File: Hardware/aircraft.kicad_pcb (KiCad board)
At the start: 4 copper layers, 131 parts, among them U1 MIC26903YJL-TR, U10 BMP390, U12 STM32F405RGTx, U14 24CW1280T-I/OT, U15 PCA9685PW_118, U16 CH330N, U17 CH330N, U2 LD39200PU33R, U3 INA226, U4 STM32F405RGTx, U5 IST8310, U6 NEO-M8N, U7 BMI088, U8 TMP100, U9 24CW1280T-I/OT

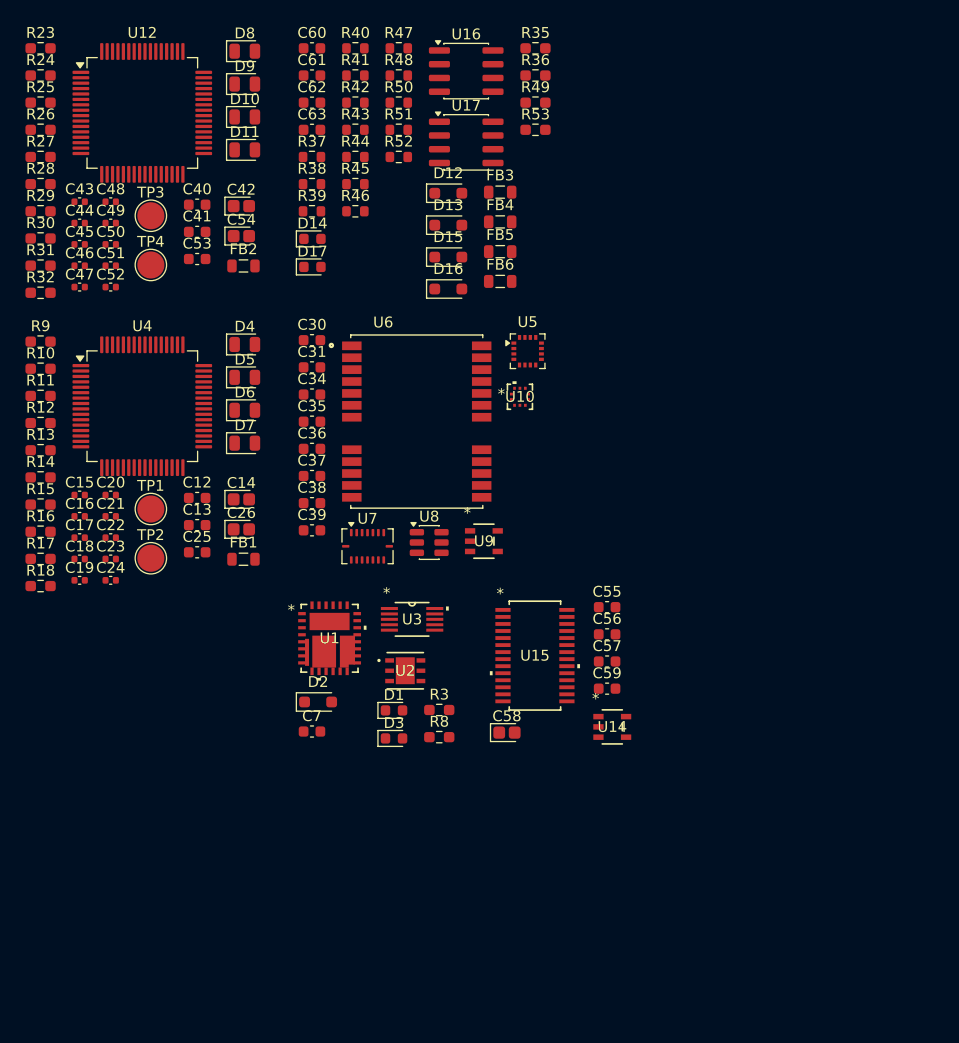
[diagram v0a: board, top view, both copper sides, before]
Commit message: hardware version 0.1.2, minor improvements and footprint selection (missing some gnss and bulk regulator components
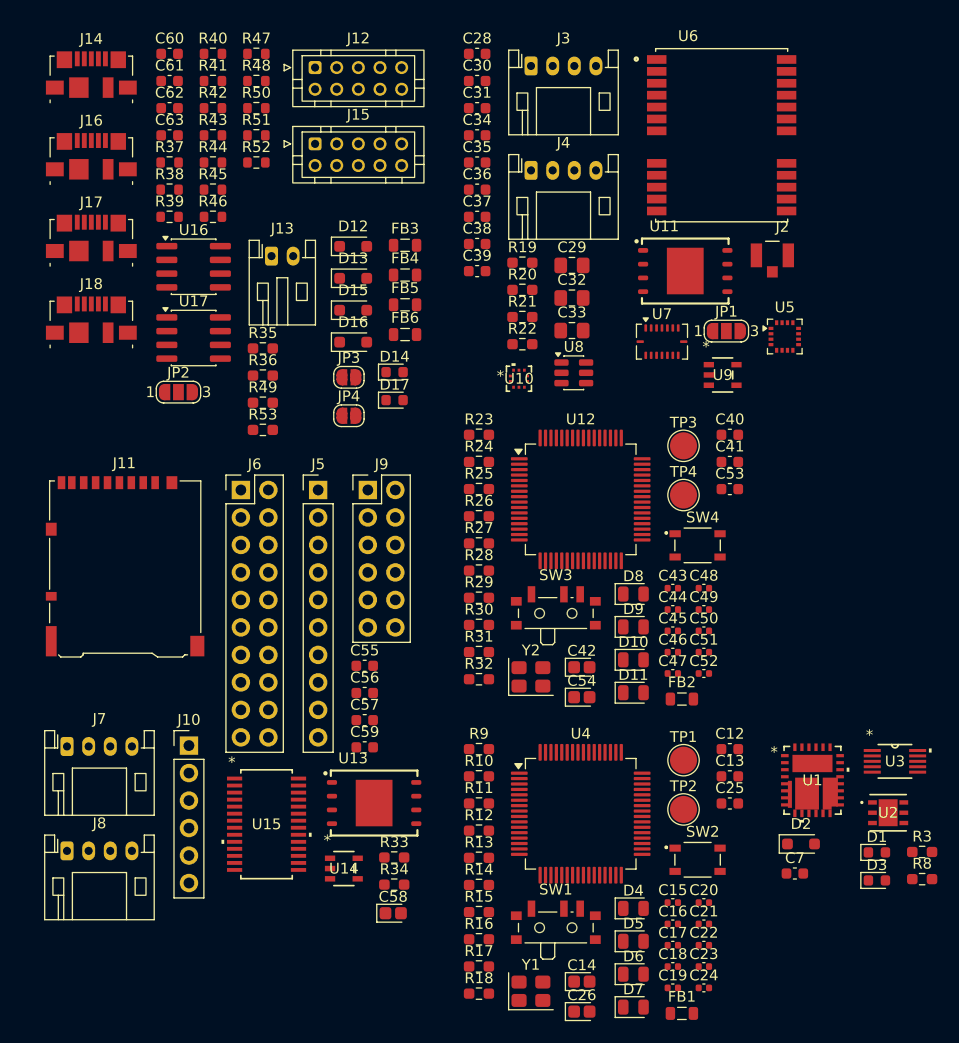
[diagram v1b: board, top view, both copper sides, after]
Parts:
- added C28: 22p, Capacitor_SMD:C_0603_1608Metric, F.Cu at (66.0, 21.7)
- added C29: 4u7, Capacitor_SMD:C_0805_2012Metric_Pad1.18x1.45mm_HandSolder, F.Cu at (74.7, 41.3)
- added C32: 1u, Capacitor_SMD:C_0805_2012Metric_Pad1.18x1.45mm_HandSolder, F.Cu at (74.7, 44.3)
- added C33: 1u, Capacitor_SMD:C_0805_2012Metric_Pad1.18x1.45mm_HandSolder, F.Cu at (74.7, 47.3)
- added J10: Conn_01x06, Connector_PinHeader_2.54mm:PinHeader_1x06_P2.54mm_Vertical, F.Cu at (39.3, 85.7)
- added J11: Micro_SD_Card_Det1, Connector_Card:microSD_HC_Hirose_DM3AT-SF-PEJM5, F.Cu at (33.4, 69.1)
- added J12: Conn_02x05_Odd_Even, Aircraft_Footprints:JST_PHD_B10B-PHDSS_2x05_P2.00mm_Vertical, F.Cu at (51.0, 23.0)
- added J13: Conn_01x02, Connector_JST:JST_PH_S2B-PH-K_1x02_P2.00mm_Horizontal, F.Cu at (47.0, 40.4)
- added J14: USB_B_Micro, Connector_USB:USB_Micro-B_Molex_47346-0001, F.Cu at (30.3, 23.7)
- added J15: Conn_02x05_Odd_Even, Aircraft_Footprints:JST_PHD_B10B-PHDSS_2x05_P2.00mm_Vertical, F.Cu at (51.0, 30.1)
- added J16: USB_B_Micro, Connector_USB:USB_Micro-B_Molex_47346-0001, F.Cu at (30.3, 31.2)
- added J17: USB_B_Micro, Connector_USB:USB_Micro-B_Molex_47346-0001, F.Cu at (30.3, 38.8)
- added J18: USB_B_Micro, Connector_USB:USB_Micro-B_Molex_47346-0001, F.Cu at (30.3, 46.3)
- added J2: 5-1814832-1, Aircraft_Footprints:HIROSE_U.FL-R-SMT-1_80_, F.Cu at (93.2, 40.4)
- added J3: Conn_01x04, Connector_JST:JST_PH_S4B-PH-K_1x04_P2.00mm_Horizontal, F.Cu at (70.9, 22.9)
- added J4: Conn_01x04, Connector_JST:JST_PH_S4B-PH-K_1x04_P2.00mm_Horizontal, F.Cu at (70.9, 32.5)
- added J5: Conn_01x10, Connector_PinHeader_2.54mm:PinHeader_1x10_P2.54mm_Vertical, F.Cu at (51.3, 62.0)
- added J6: Conn_02x10_Odd_Even, Connector_PinHeader_2.54mm:PinHeader_2x10_P2.54mm_Vertical, F.Cu at (44.1, 62.0)
- added J7: Conn_01x04, Connector_JST:JST_PH_S4B-PH-K_1x04_P2.00mm_Horizontal, F.Cu at (28.1, 85.7)
- added J8: Conn_01x04, Connector_JST:JST_PH_S4B-PH-K_1x04_P2.00mm_Horizontal, F.Cu at (28.1, 95.4)
- added J9: Conn_02x06_Odd_Even, Connector_PinHeader_2.54mm:PinHeader_2x06_P2.54mm_Vertical, F.Cu at (55.9, 62.0)
- added JP1: SolderJumper_3_Open, Jumper:SolderJumper-3_P1.3mm_Open_RoundedPad1.0x1.5mm_NumberLabels, F.Cu at (89.0, 47.4)
- added JP2: Jumper_3_Open, Jumper:SolderJumper-3_P1.3mm_Open_RoundedPad1.0x1.5mm_NumberLabels, F.Cu at (38.4, 53.0)
- added JP3: SolderJumper_2_Open, Jumper:SolderJumper-2_P1.3mm_Open_RoundedPad1.0x1.5mm, F.Cu at (54.1, 51.6)
- added JP4: SolderJumper_2_Open, Jumper:SolderJumper-2_P1.3mm_Open_RoundedPad1.0x1.5mm, F.Cu at (54.1, 55.2)
- added R19: 10, Resistor_SMD:R_0603_1608Metric_Pad0.98x0.95mm_HandSolder, F.Cu at (70.1, 41.0)
- added R20: 10k, Resistor_SMD:R_0603_1608Metric_Pad0.98x0.95mm_HandSolder, F.Cu at (70.1, 43.5)
- added R21: 10k, Resistor_SMD:R_0603_1608Metric_Pad0.98x0.95mm_HandSolder, F.Cu at (70.1, 46.1)
- added R22: 10k, Resistor_SMD:R_0603_1608Metric_Pad0.98x0.95mm_HandSolder, F.Cu at (70.1, 48.6)
- added R33: 10k, Resistor_SMD:R_0603_1608Metric_Pad0.98x0.95mm_HandSolder, F.Cu at (58.3, 96.0)
- added R34: 10k, Resistor_SMD:R_0603_1608Metric_Pad0.98x0.95mm_HandSolder, F.Cu at (58.3, 98.5)
- added SW1: SW_SPDT, Button_Switch_SMD:SW_SPDT_PCM12, F.Cu at (73.2, 102.2)
- added SW2: SW_Push_Dual, Aircraft_Footprints:SW_SKRPACE010, F.Cu at (86.3, 96.2)
- added SW3: SW_SPDT, Button_Switch_SMD:SW_SPDT_PCM12, F.Cu at (73.2, 73.1)
- added SW4: SW_Push_Dual, Aircraft_Footprints:SW_SKRPACE010, F.Cu at (86.3, 67.2)
- added U11: W25N01GVZEIG_TR, Aircraft_Footprints:SON127P800X600X80-9N, F.Cu at (85.2, 41.8)
- added U13: W25N01GVZEIG_TR, Aircraft_Footprints:SON127P800X600X80-9N, F.Cu at (56.4, 91.0)
- added Y1: 25MHz, Crystal:Crystal_SMD_Abracon_ABM8G-4Pin_3.2x2.5mm, F.Cu at (70.9, 108.4)
- added Y2: 25MHz, Crystal:Crystal_SMD_Abracon_ABM8G-4Pin_3.2x2.5mm, F.Cu at (70.9, 79.3)
- moved C15 66.5 mm to (84.0, 100.2)
- moved C20 66.5 mm to (86.9, 100.2)
- moved C16 66.5 mm to (84.0, 102.1)
- moved C17 66.5 mm to (84.0, 104.1)
- moved C18 66.5 mm to (84.0, 106.1)
- moved C19 66.5 mm to (84.0, 108.0)
- moved C21 66.5 mm to (86.9, 102.1)
- moved C22 66.5 mm to (86.9, 104.1)
- moved C23 66.5 mm to (86.9, 106.1)
- moved C24 66.5 mm to (86.9, 108.0)
- moved C43 65.4 mm to (84.0, 71.1)
- moved C44 65.4 mm to (84.0, 73.1)
- moved C45 65.4 mm to (84.0, 75.1)
- moved C46 65.4 mm to (84.0, 77.0)
- moved C47 65.4 mm to (84.0, 79.0)
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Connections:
- U6 pad 7: unconnected-(U6-VDD_USB-Pad7) -> PS_PVIN

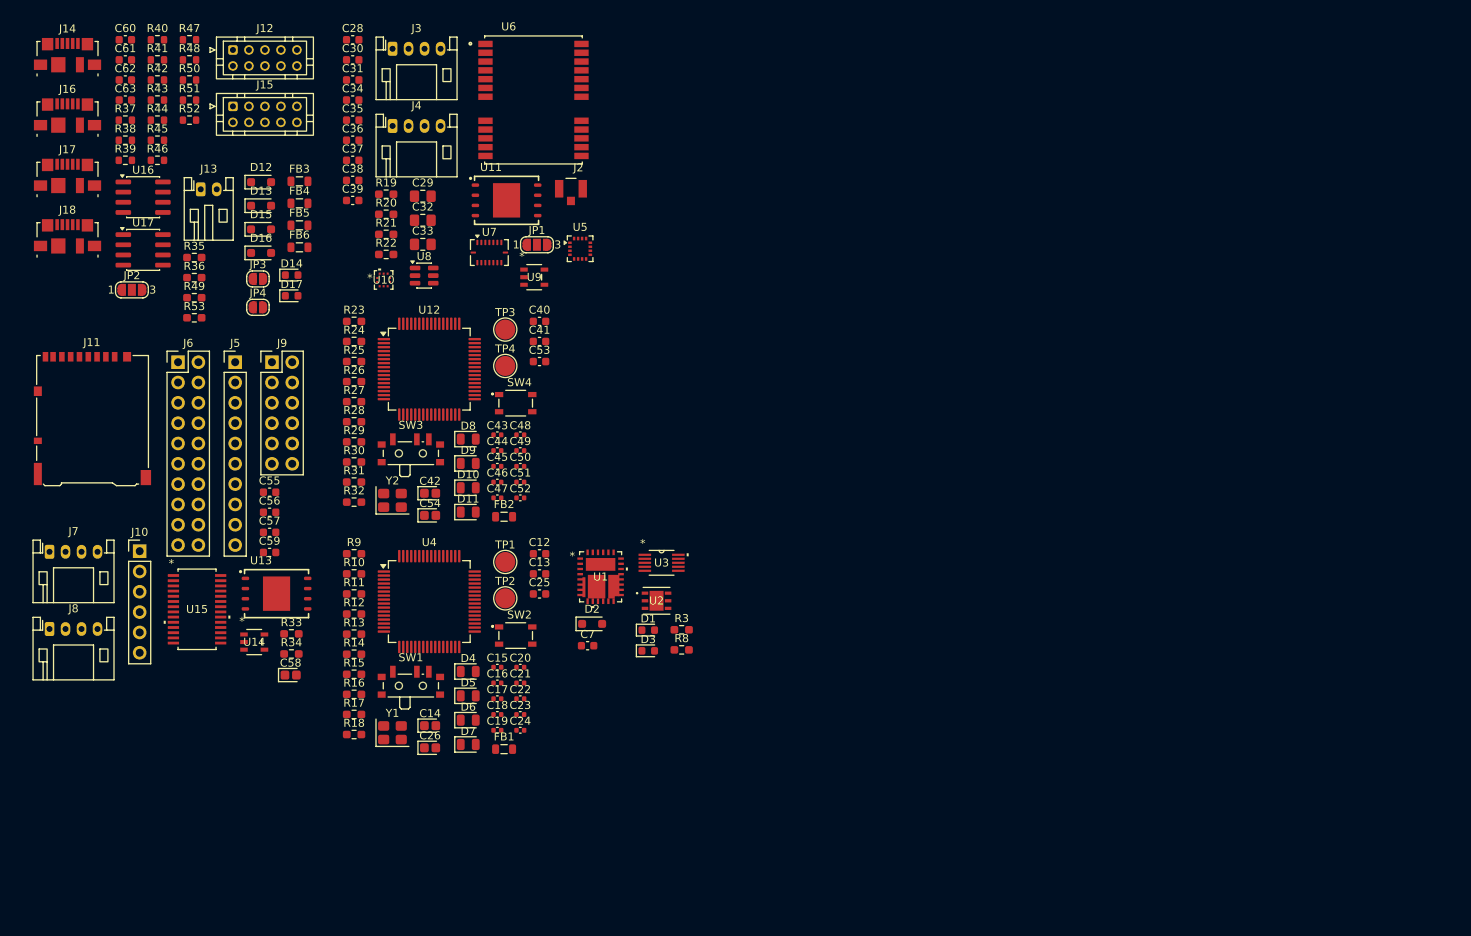
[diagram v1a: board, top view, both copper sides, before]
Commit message: board placement, no trails, just pain
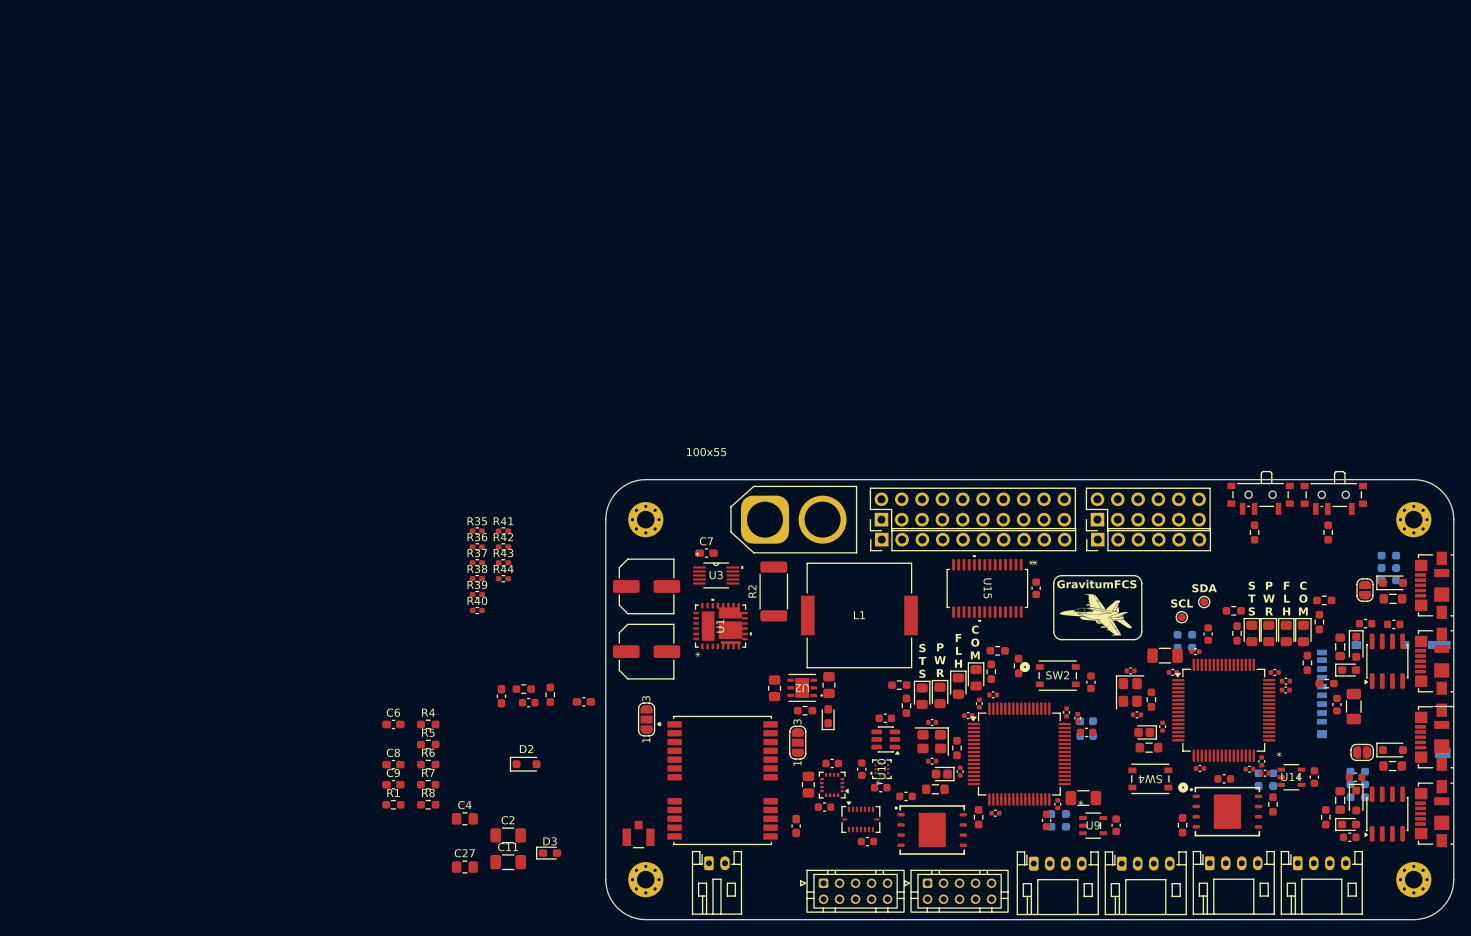
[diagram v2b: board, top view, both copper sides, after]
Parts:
- removed J11: Micro_SD_Card_Det1, Connector_Card:microSD_HC_Hirose_DM3AT-SF-PEJM5
- removed R45: 10, Resistor_SMD:R_0603_1608Metric
- removed TP1, TP2: I2C1, TestPoint:TestPoint_Pad_D2.5mm
- added C1: 100u, Capacitor_SMD:C_Elec_6.3x7.7, F.Cu at (102.7, 90.1)
- added C10: 100u, Capacitor_SMD:C_Elec_6.3x7.7, F.Cu at (102.7, 98.2)
- added C11: 47u, Capacitor_SMD:C_1206_3216Metric_Pad1.33x1.80mm_HandSolder, F.Cu at (85.4, 124.5)
- added C2: 47u, Capacitor_SMD:C_1206_3216Metric_Pad1.33x1.80mm_HandSolder, F.Cu at (85.4, 121.2)
- added C27: 2u2, Capacitor_SMD:C_0805_2012Metric_Pad1.18x1.45mm_HandSolder, F.Cu at (80.0, 125.1)
- added C3: 10u, Capacitor_SMD:C_0805_2012Metric_Pad1.18x1.45mm_HandSolder, F.Cu at (118.7, 102.8)
- added C4: 2u2, Capacitor_SMD:C_0805_2012Metric_Pad1.18x1.45mm_HandSolder, F.Cu at (80.0, 119.1)
- added C5: 10u, Capacitor_SMD:C_0805_2012Metric_Pad1.18x1.45mm_HandSolder, F.Cu at (125.5, 102.4)
- added C6: 100n, Capacitor_SMD:C_0603_1608Metric_Pad1.08x0.95mm_HandSolder, F.Cu at (71.1, 107.3)
- added C8: 100n, Capacitor_SMD:C_0603_1608Metric_Pad1.08x0.95mm_HandSolder, F.Cu at (71.1, 112.3)
- added C9: 4n7, Capacitor_SMD:C_0603_1608Metric_Pad1.08x0.95mm_HandSolder, F.Cu at (71.1, 114.8)
- added G***: LOGO, LOGO, F.Cu at (159.1, 93.6)
- added G***: LOGO, LOGO, B.Cu at (150.2, 98.5)
- added J1: Conn_01x02_Pin, Connector_AMASS:AMASS_XT60-M_1x02_P7.20mm_Vertical, F.Cu at (117.5, 81.7)
- added J19: U.FL-R-SMT-1_80_, Aircraft_Footprints:HIROSE_U.FL-R-SMT-1_80_, F.Cu at (101.7, 121.4)
- added L1: 15u, Aircraft_Footprints:IND_PA4343_FOOTPRINT2_PUL, F.Cu at (129.3, 93.7)
- added L2: 27n, Inductor_SMD:L_0603_1608Metric_Pad1.05x0.95mm_HandSolder, F.Cu at (84.6, 103.8)
- added R1: 10k, Resistor_SMD:R_0603_1608Metric_Pad0.98x0.95mm_HandSolder, F.Cu at (71.1, 117.4)
- added R2: 10m, Resistor_SMD:R_2512_6332Metric_Pad1.40x3.35mm_HandSolder, F.Cu at (118.6, 90.7)
- added R4: 10k, Resistor_SMD:R_0603_1608Metric_Pad0.98x0.95mm_HandSolder, F.Cu at (75.4, 107.3)
- added R5: 19k6, Resistor_SMD:R_0603_1608Metric_Pad0.98x0.95mm_HandSolder, F.Cu at (75.4, 109.8)
- added R54: 10k, Resistor_SMD:R_0603_1608Metric_Pad0.98x0.95mm_HandSolder, F.Cu at (185.3, 99.6)
- added R6: 6k8, Resistor_SMD:R_0603_1608Metric_Pad0.98x0.95mm_HandSolder, F.Cu at (75.4, 112.3)
- added R7: 1k3, Resistor_SMD:R_0603_1608Metric_Pad0.98x0.95mm_HandSolder, F.Cu at (75.4, 114.8)
- added REF**: MountingHole_2.2mm_M2_Pad_Via, MountingHole:MountingHole_2.2mm_M2_Pad_Via, F.Cu at (198.6, 126.7)
- added REF**: MountingHole_2.2mm_M2_Pad_Via, MountingHole:MountingHole_2.2mm_M2_Pad_Via, F.Cu at (102.6, 126.7)
- added REF**: MountingHole_2.2mm_M2_Pad_Via, MountingHole:MountingHole_2.2mm_M2_Pad_Via, F.Cu at (198.6, 81.7)
- added REF**: MountingHole_2.2mm_M2_Pad_Via, MountingHole:MountingHole_2.2mm_M2_Pad_Via, F.Cu at (102.6, 81.7)
- C14, C42: footprint Capacitor_Tantalum_SMD:CP_EIA-1608-08_AVX-J -> Capacitor_SMD:C_1206_3216Metric_Pad1.33x1.80mm_HandSolder
- C32, C33: footprint Capacitor_SMD:C_0805_2012Metric_Pad1.18x1.45mm_HandSolder -> Capacitor_SMD:C_0603_1608Metric_Pad1.08x0.95mm_HandSolder
- C40, C41: footprint Capacitor_SMD:C_0603_1608Metric -> Capacitor_SMD:C_0402_1005Metric
- C57: value 100n -> 10u; footprint Capacitor_SMD:C_0603_1608Metric -> Capacitor_SMD:C_1206_3216Metric_Pad1.33x1.80mm_HandSolder
- C58: value 10u -> 100n; footprint Capacitor_Tantalum_SMD:CP_EIA-1608-08_AVX-J -> Capacitor_SMD:C_0603_1608Metric
- C7: footprint Capacitor_SMD:C_0603_1608Metric -> Capacitor_SMD:C_0603_1608Metric_Pad1.08x0.95mm_HandSolder
- D1, D14, D17, D3: footprint LED_SMD:LED_0603_1608Metric -> LED_SMD:LED_0603_1608Metric_Pad1.05x0.95mm_HandSolder
- D10, D11, D4, D5, D6, D7, D8, D9: footprint LED_SMD:LED_0805_2012Metric -> LED_SMD:LED_0805_2012Metric_Pad1.15x1.40mm_HandSolder
- FB1, FB2, FB3, FB4, FB5, FB6: footprint Inductor_SMD:L_0805_2012Metric -> Inductor_SMD:L_0805_2012Metric_Pad1.05x1.20mm_HandSolder
- J2: value 5-1814832-1 -> DM3AT-SF-PEJM5; footprint Aircraft_Footprints:HIROSE_U.FL-R-SMT-1_80_ -> Aircraft_Footprints:HRS_DM3AT-SF-PEJM5; moved to B.Cu
- R15, R16, R17, R18, R29, R30, R31, R32: moved to B.Cu
- R35, R36: footprint Resistor_SMD:R_0603_1608Metric_Pad0.98x0.95mm_HandSolder -> Resistor_SMD:R_0402_1005Metric_Pad0.72x0.64mm_HandSolder
- R37, R38, R39, R40, R41, R42, R43, R44: footprint Resistor_SMD:R_0603_1608Metric -> Resistor_SMD:R_0402_1005Metric_Pad0.72x0.64mm_HandSolder
- R46, R47, R48, R50, R51, R52: footprint Resistor_SMD:R_0603_1608Metric -> Resistor_SMD:R_0603_1608Metric_Pad0.98x0.95mm_HandSolder; moved to B.Cu
- SW2, SW4: footprint Aircraft_Footprints:SW_SKRPACE010 -> Aircraft_Footprints:SW4_PTS815 SJM 250 SMTR LFS_CNK
- TP3, TP4: footprint TestPoint:TestPoint_Pad_D2.5mm -> TestPoint:TestPoint_Pad_D1.0mm
- moved J14 195.2 mm to (200.9, 118.5), turned to 90 degrees
- moved J16 187.4 mm to (200.9, 108.9), turned to 90 degrees
- moved C61 181.3 mm to (190.6, 121.4), turned to 180 degrees
- moved J17 181.0 mm to (200.9, 99.4), turned to 90 degrees
- moved C60 179.3 mm to (191.3, 113.9), turned to 180 degrees
- moved J18 176.1 mm to (200.9, 89.9), turned to 90 degrees
- moved R47 174.1 mm to (191.6, 116.4), turned to 180 degrees
- moved U16 173.6 mm to (195.3, 118.5), turned to 90 degrees
- moved C63 171.6 mm to (196.1, 94.8), turned to 180 degrees
- moved R48 171.0 mm to (191.6, 113.2), turned to 180 degrees
- moved C62 169.3 mm to (192.6, 94.7), turned to 180 degrees
- moved R46 169.1 mm to (191.6, 114.8), turned to 180 degrees
- moved U17 163.8 mm to (195.3, 99.4), turned to 90 degrees
- moved R50 161.9 mm to (195.5, 87.8), turned to 180 degrees
- moved R51 161.5 mm to (195.5, 89.3), turned to 180 degrees
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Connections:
- net FCU_GPIOA renamed FCU_GPIO_A
- net FCU_GPIOB renamed FCU_GPIO_B
- net FCU_GPIOC renamed FCU_GPIO_C
- net FCU_GPIOD renamed FCU_GPIO_D
- net FCU_GPIOE renamed FCU_GPIO_E
- net FCU_GPIOF renamed FCU_GPIO_F
- C12 pad 2: PS_PVIN -> GND
- C13 pad 2: PS_PVIN -> GND
- C14 pad 2: PS_PVIN -> GND
- C15 pad 2: PS_PVIN -> GND
- C16 pad 2: PS_PVIN -> GND
- C17 pad 2: PS_PVIN -> GND
- C18 pad 2: PS_PVIN -> GND
- C19 pad 2: PS_PVIN -> GND
- C20 pad 2: PS_PVIN -> GND
- C21 pad 2: PS_PVIN -> GND
- C22 pad 2: PS_PVIN -> GND
- C23 pad 2: PS_PVIN -> GND
- C24 pad 2: PS_PVIN -> GND
- C25 pad 2: PS_PVIN -> GND
- C26 pad 2: PS_PVIN -> GND
- C28 pad 1: PS_PVIN -> GND
- C29 pad 1: PS_PVIN -> GND
- C30 pad 2: PS_PVIN -> GND
- C31 pad 2: PS_PVIN -> GND
- C32 pad 1: PS_PVIN -> GND
- C33 pad 1: PS_PVIN -> GND
- C34 pad 2: PS_PVIN -> GND
- C35 pad 1: PS_PVIN -> GND
- C36 pad 2: PS_PVIN -> GND
- C37 pad 1: PS_PVIN -> GND
- C38 pad 1: PS_PVIN -> GND
- C39 pad 2: PS_PVIN -> GND
- C40 pad 2: PS_PVIN -> GND
- C41 pad 2: PS_PVIN -> GND
- C42 pad 2: PS_PVIN -> GND
- C43 pad 2: PS_PVIN -> GND
- C44 pad 2: PS_PVIN -> GND
- C45 pad 2: PS_PVIN -> GND
- C46 pad 2: PS_PVIN -> GND
- C47 pad 2: PS_PVIN -> GND
- C48 pad 2: PS_PVIN -> GND
- C49 pad 2: PS_PVIN -> GND
- C50 pad 2: PS_PVIN -> GND
- C51 pad 2: PS_PVIN -> GND
- C52 pad 2: PS_PVIN -> GND
- C53 pad 2: PS_PVIN -> GND
- C54 pad 2: PS_PVIN -> GND
- C55 pad 2: PS_PVIN -> GND
- C56 pad 2: PS_PVIN -> GND
- C57 pad 2: PS_PVIN -> GND
- C58 pad 2: PS_PVIN -> GND
- C59 pad 2: PS_PVIN -> GND
- C60 pad 2: PS_PVIN -> GND
- C61 pad 2: PS_PVIN -> GND
- C62 pad 2: PS_PVIN -> GND
- C63 pad 2: PS_PVIN -> GND
- C7 pad 2: PS_PVIN -> GND
- D1 pad 1: PS_PVIN -> GND
- D3 pad 1: PS_PVIN -> GND
- D4 pad 2: NU_LED4 -> NU_LED_4
- D5 pad 2: NU_LED3 -> NU_LED_3
- D6 pad 2: NU_LED2 -> NU_LED_2
- D7 pad 2: NU_LED1 -> NU_LED_1
- J12 pad 3: PS_PVIN -> GND
- J12 pad 4: PS_PVIN -> GND
- J13 pad 2: PS_PVIN -> GND
- J14 pad 5: PS_PVIN -> GND
- J14 pad 6: PS_PVIN -> GND
- J15 pad 3: PS_PVIN -> GND
- J15 pad 4: PS_PVIN -> GND
- J16 pad 5: PS_PVIN -> GND
- J16 pad 6: PS_PVIN -> GND
- J17 pad 5: PS_PVIN -> GND
- J17 pad 6: PS_PVIN -> GND
- J18 pad 5: PS_PVIN -> GND
- J18 pad 6: PS_PVIN -> GND
- J3 pad 2: PS_PVIN -> GND
- J4 pad 2: PS_PVIN -> GND
- J6 pad 10: PS_PVIN -> GND
- J6 pad 12: PS_PVIN -> GND
- J6 pad 14: PS_PVIN -> GND
- J6 pad 16: PS_PVIN -> GND
- J6 pad 18: PS_PVIN -> GND
- J6 pad 2: PS_PVIN -> GND
- J6 pad 20: PS_PVIN -> GND
- J6 pad 4: PS_PVIN -> GND
- J6 pad 6: PS_PVIN -> GND
- J6 pad 8: PS_PVIN -> GND
- J7 pad 2: PS_PVIN -> GND
- J8 pad 2: PS_PVIN -> GND
- J9 pad 10: PS_PVIN -> GND
- J9 pad 12: PS_PVIN -> GND
- J9 pad 2: PS_PVIN -> GND
- J9 pad 4: PS_PVIN -> GND
- J9 pad 6: PS_PVIN -> GND
- J9 pad 8: PS_PVIN -> GND
- JP1 pad 3: PS_PVIN -> GND
- R12 pad 2: PS_PVIN -> GND
- R13 pad 2: PS_PVIN -> GND
- R14 pad 2: PS_PVIN -> GND
- R23 pad 2: PS_PVIN -> GND
- R26 pad 2: PS_PVIN -> GND
- R27 pad 2: PS_PVIN -> GND
- R28 pad 2: PS_PVIN -> GND
- R35 pad 2: NU_I2C2_SDA -> NU_I2C1_SDA
- R36 pad 2: NU_I2C2_SCL -> NU_I2C1_SCL
- R39 pad 2: NU_GPIOA -> NU_GPIO_A
- R40 pad 2: NU_GPIOB -> NU_GPIO_B
- R41 pad 2: NU_GPIOC -> NU_GPIO_C
- R42 pad 2: NU_GPIOD -> NU_GPIO_D
- R43 pad 2: NU_GPIOE -> NU_GPIO_E
- R44 pad 2: NU_GPIOF -> NU_GPIO_F
- R49 pad 2: PS_PVIN -> GND
- R53 pad 2: PS_PVIN -> GND
- R9 pad 2: PS_PVIN -> GND
- SW1 pad 3: PS_PVIN -> GND
- SW2 pad 1: PS_PVIN -> GND
- SW2 pad 3: PS_PVIN -> GND
- SW3 pad 3: PS_PVIN -> GND
- SW4 pad 1: PS_PVIN -> GND
- SW4 pad 3: PS_PVIN -> GND
- U1 pad 2: PS_PVIN -> GND
- U1 pad 21: PS_PVIN -> GND
- U1 pad 23: PS_PVIN -> GND
- U1 pad 29: PS_PVIN -> GND
- U1 pad 5: PS_PVIN -> GND
- U1 pad 6: PS_PVIN -> GND
- U1 pad 7: PS_PVIN -> GND
- U1 pad 8: PS_PVIN -> GND
- U10 pad 3: PS_PVIN -> GND
- U10 pad 5: PS_PVIN -> GND
- U10 pad 8: PS_PVIN -> GND
- U10 pad 9: PS_PVIN -> GND
- U11 pad 4: PS_PVIN -> GND
- U12 pad 12: PS_PVIN -> GND
- U12 pad 18: PS_PVIN -> GND
- U12 pad 20: FCU_SP1_FLASH_CS -> FCU_SPI1_FLASH_CS
- U12 pad 63: PS_PVIN -> GND
- U13 pad 4: PS_PVIN -> GND
- U14 pad 2: PS_PVIN -> GND
- U15 pad 14: PS_PVIN -> GND
- U15 pad 2: PS_PVIN -> GND
- U15 pad 23: PS_PVIN -> GND
- U15 pad 24: PS_PVIN -> GND
- U15 pad 3: PS_PVIN -> GND
- U15 pad 4: PS_PVIN -> GND
- U15 pad 5: PS_PVIN -> GND
- U16 pad 3: PS_PVIN -> GND
- U17 pad 3: PS_PVIN -> GND
- U2 pad 3: PS_PVIN -> GND
- U2 pad 7: PS_PVIN -> GND
- U3 pad 1: PS_PVIN -> GND
- U3 pad 2: PS_PVIN -> GND
- U3 pad 7: PS_PVIN -> GND
- U4 pad 12: PS_PVIN -> GND
- U4 pad 18: PS_PVIN -> GND
- U4 pad 63: PS_PVIN -> GND
- U5 pad 11: PS_PVIN -> GND
- U5 pad 5: PS_PVIN -> GND
- U5 pad 6: PS_PVIN -> GND
- U5 pad 9: PS_PVIN -> GND
- U6 pad 10: PS_PVIN -> GND
- U6 pad 12: PS_PVIN -> GND
- U6 pad 13: PS_PVIN -> GND
- U6 pad 24: PS_PVIN -> GND
- U6 pad 7: PS_PVIN -> GND
- U7 pad 10: PS_PVIN -> GND
- U7 pad 15: PS_PVIN -> GND
- U7 pad 2: PS_PVIN -> GND
- U7 pad 4: PS_PVIN -> GND
- U7 pad 6: PS_PVIN -> GND
- U8 pad 2: PS_PVIN -> GND
- U8 pad 3: PS_PVIN -> GND
- U8 pad 5: PS_PVIN -> GND
- U9 pad 2: PS_PVIN -> GND
- Y1 pad 2: PS_PVIN -> GND
- Y1 pad 4: PS_PVIN -> GND
- Y2 pad 2: PS_PVIN -> GND
- Y2 pad 4: PS_PVIN -> GND
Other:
- board outline added: 106.1 x 55 mm
- board text added: "100x55"
- board text added: "C O M"
- board text added: "F L H"
- board text added: "FlyCU"
- board text added: "GravitumFCS"
- board text added: "Made by Breno Soares Alves"
- board text added: "P W R"
- board text added: "S T S"
- board text added: "SCL"
- board text added: "SDA"
